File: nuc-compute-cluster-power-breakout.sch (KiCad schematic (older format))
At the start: 9 parts, among them J2 BM04B-SRSS-TB-LF-SN, J3 BM04B-SRSS-TB-LF-SN, J5 430450812, J6 430450812, J7 430450812, J8 430450812, J9 430450812

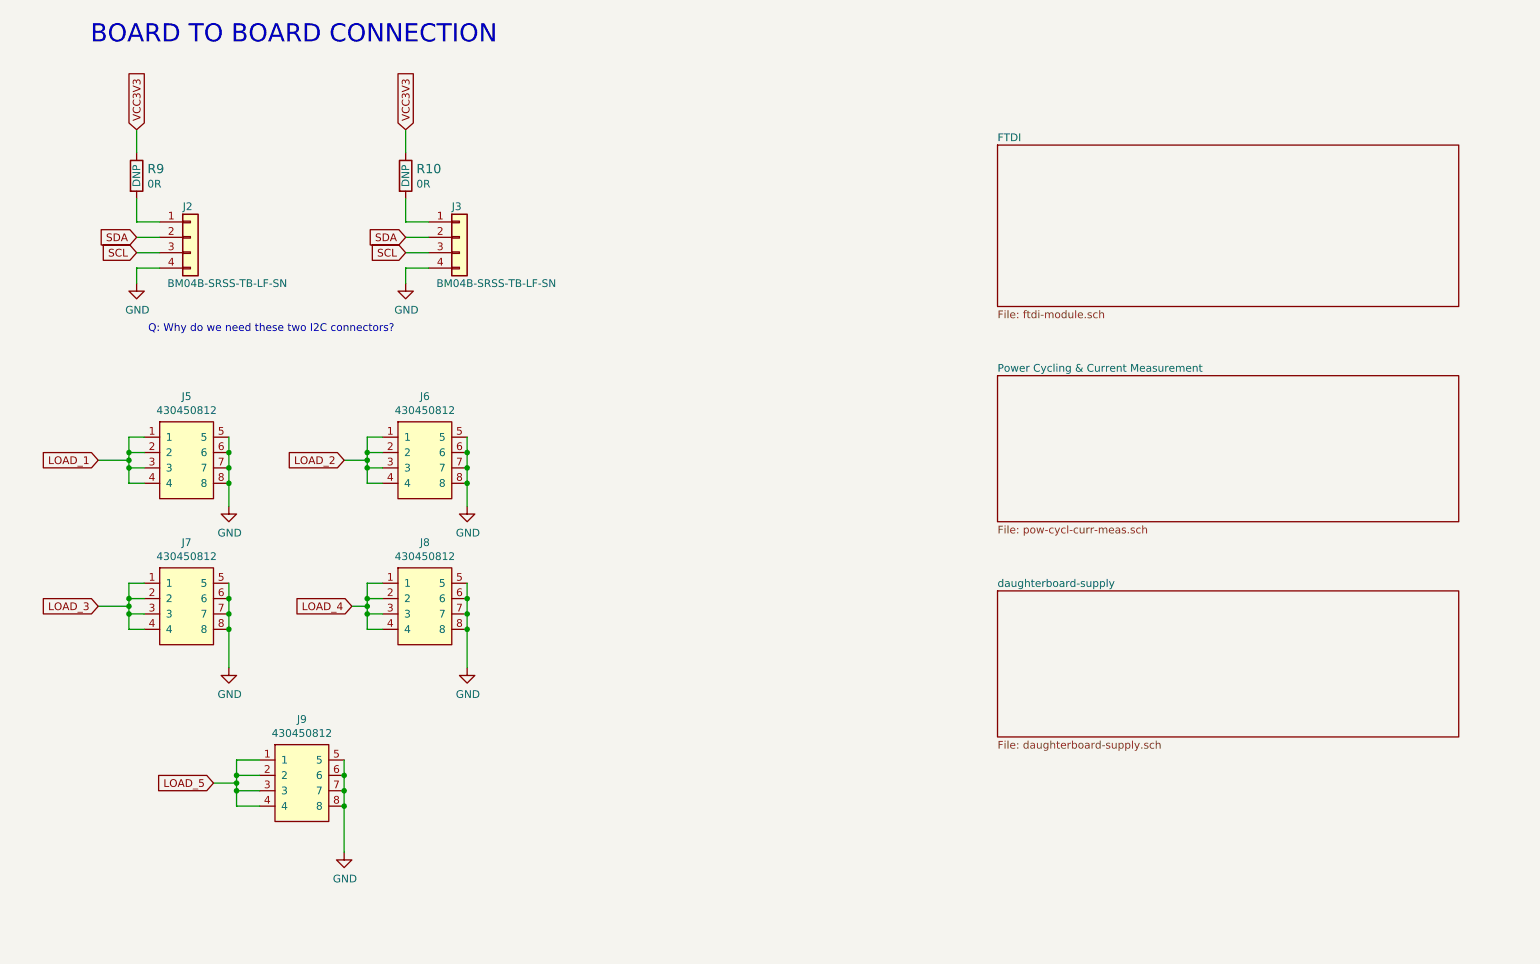
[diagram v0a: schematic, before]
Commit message: Added PSU power on switch
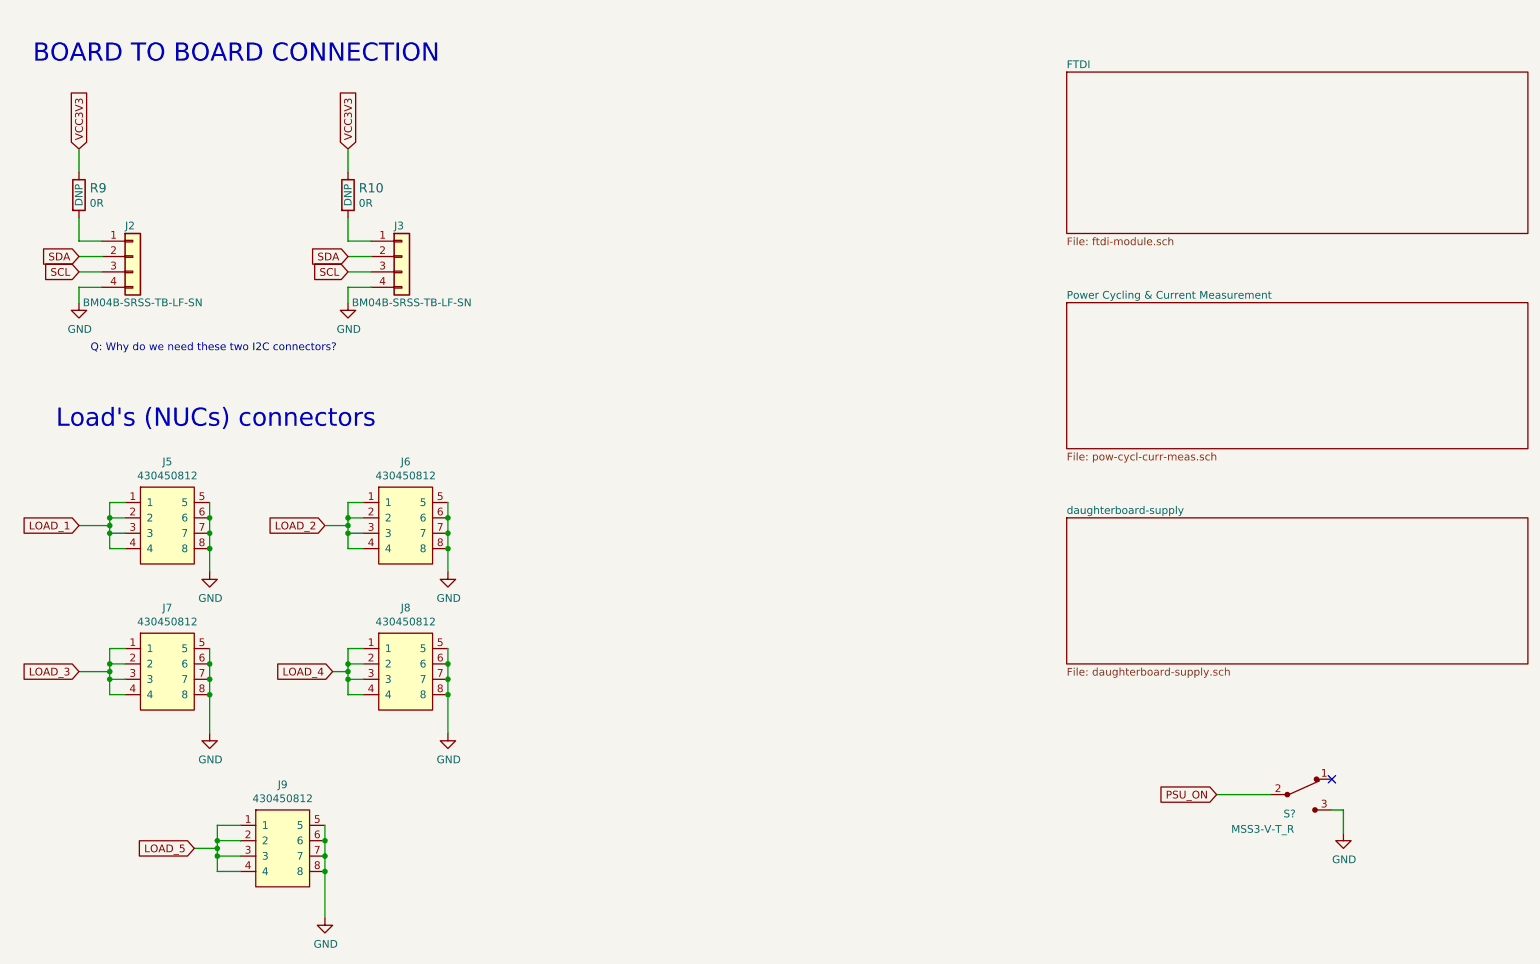
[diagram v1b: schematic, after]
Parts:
- added S?: MSS3-V-T_R, antmicro-footprints:Switch_Slide_MSS3, symbol antmicroSlideSwitches:MSS3-V-T_R
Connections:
- net GND: now also S?.3
- new net PSU_ON: S?.2
- no-connect marks 0 -> 1
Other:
- note added: "Load's (NUCs) connectors"
- moved on the sheet: J2, J3, J5, J6, J7, J8, J9, R10, R9

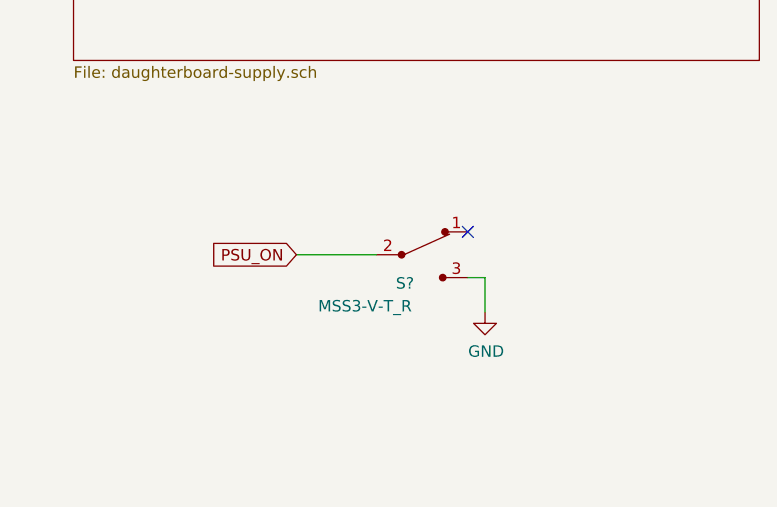
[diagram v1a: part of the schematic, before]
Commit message: FTDI layout redesign
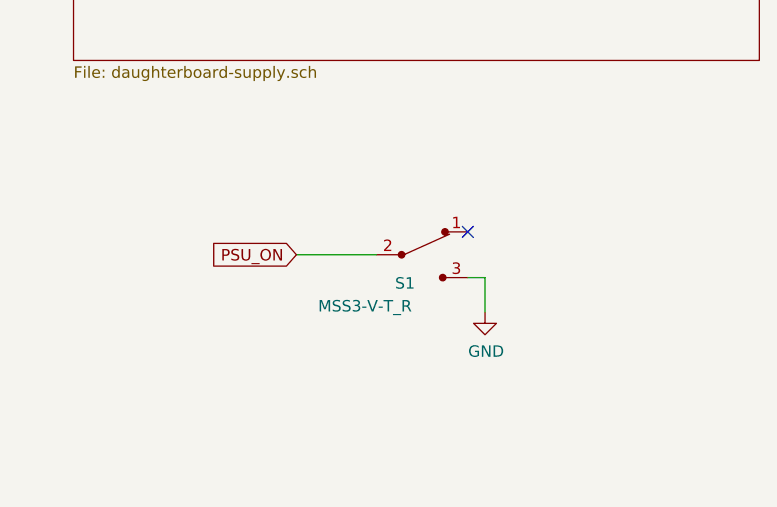
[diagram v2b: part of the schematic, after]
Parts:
- gave numbers to parts that had none: 1
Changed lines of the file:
@@
 PSU_ON
 $Comp
-L nuc-compute-cluster-power-breakout:GND #PWR?
+L nuc-compute-cluster-power-breakout:GND #PWR0102
 U 1 1 62727538
 P 9650 5875
-F 0 "#PWR?" H 9650 5625 50  0001 C CNN
+F 0 "#PWR0102" H 9650 5625 50  0001 C CNN
 F 1 "GND" H 9655 5702 50  0000 C CNN
 F 2 "" H 9650 5875 50  0001 C CNN
@@
 	9650 5725 9575 5725
 $Comp
-L antmicroSlideSwitches:MSS3-V-T_R S?
+L antmicroSlideSwitches:MSS3-V-T_R S1
 U 1 1 6270AED7
 P 9375 5625
-F 0 "S?" H 9300 5500 50  0000 C CNN
+F 0 "S1" H 9300 5500 50  0000 C CNN
 F 1 "MSS3-V-T_R" H 9125 5400 50  0000 C CNN
 F 2 "antmicro-footprints:Switch_Slide_MSS3" H 9575 5825 50  0001 L CNN

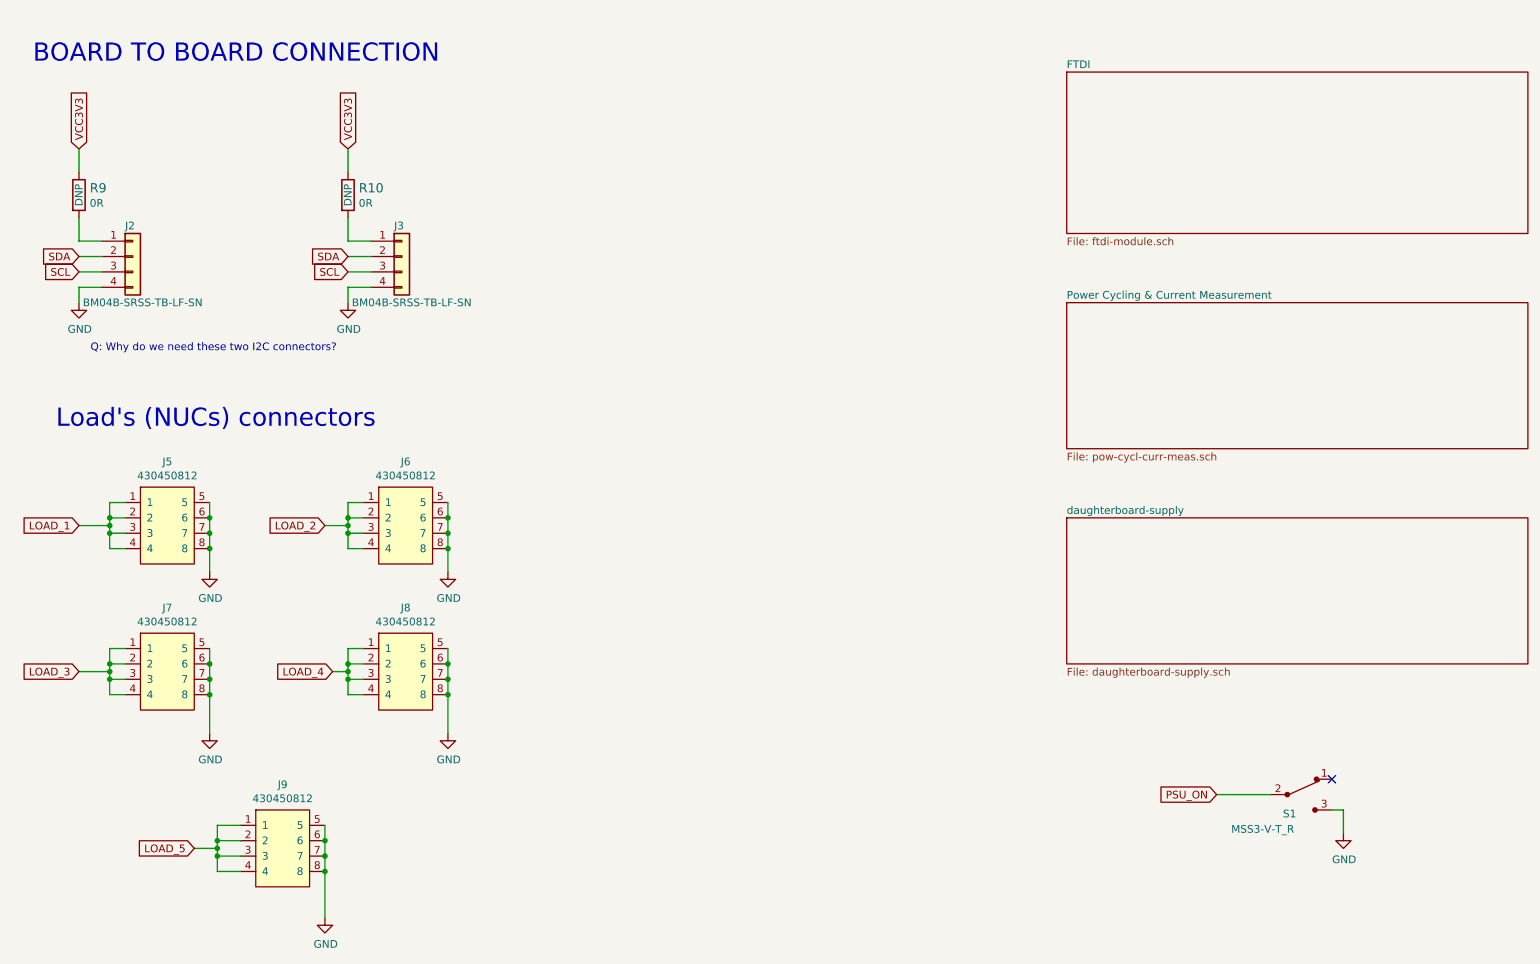
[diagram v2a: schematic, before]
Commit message: Added power switch. PCB update.
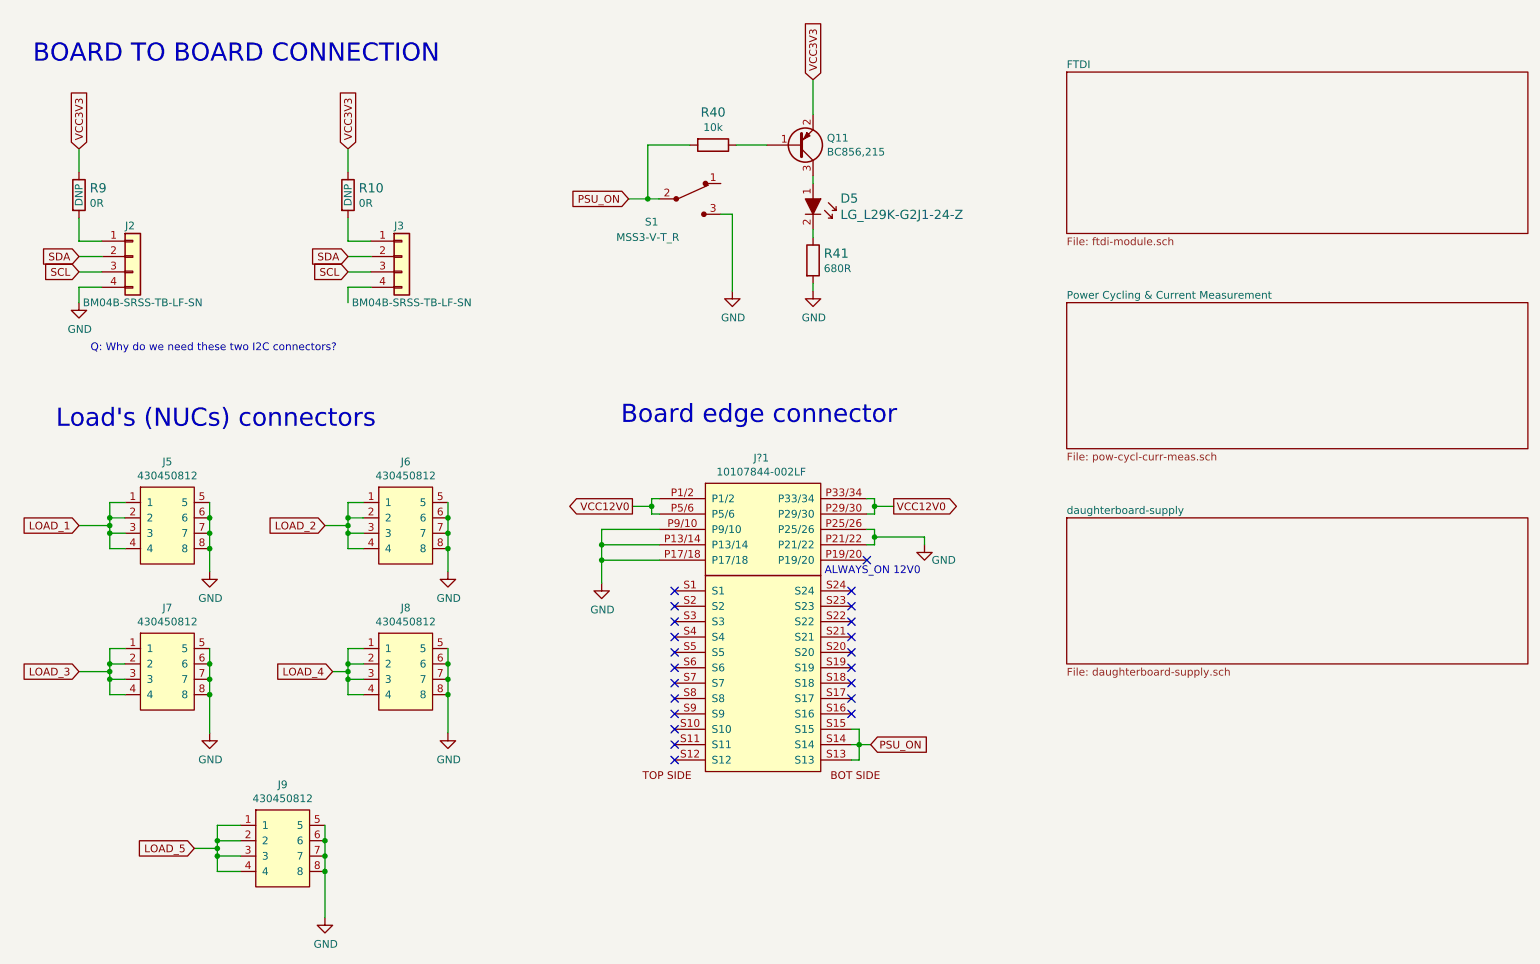
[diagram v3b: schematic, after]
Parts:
- added D5: LG_L29K-G2J1-24-Z, antmicro-footprints:LED_0603, symbol antmicroLEDIndicationDiscrete:LG_L29K-G2J1-24-Z
- added J?1: 10107844-002LF, antmicro-footprints:10107844-002LF, symbol antmicroRectangularConnectorsHeadersFemalePins:10107844-002LF
- added Q11: BC856,215, antmicro-footprints:SOT-23-3, symbol antmicroTransistorsBipolarSingle:BC856,215
- added R40: R_10k_0402, antmicro-footprints:0402-res, symbol antmicroResistors0402:R_10k_0402
- added R41: R_680R_0402, antmicro-footprints:0402-res, symbol antmicroResistors0402:R_680R_0402
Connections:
- net GND: now also J?1.P11/12, J?1.P13/14, J?1.P15/16, J?1.P17/18, J?1.P21/22, J?1.P23/24, J?1.P25/26, J?1.P27/28, J?1.P9/10, R41.2; no longer J3.4 (Pin_4)
- net PSU_ON: now also J?1.S13, J?1.S14, J?1.S15, R40.2
- net VCC3V3: now also Q11.2
- new net: D5.1, Q11.3
- new net: D5.2, R41.1
- new net: Q11.1, R40.1
- new net P3/4: J?1.P1/2, J?1.P29/30, J?1.P3/4, J?1.P31/32, J?1.P33/34, J?1.P35/36, J?1.P5/6, J?1.P7/8
- no-connect marks 1 -> 22
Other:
- note added: "ALWAYS_ON 12V0\n"
- note added: "Board edge connector\n"
- moved on the sheet: S1
